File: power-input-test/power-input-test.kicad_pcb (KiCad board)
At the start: 2 copper layers, 19 x 27.3 mm, 15 parts, among them J1 USB_C_Receptacle_USB2.0, J2 Conn_01x06, J3 Conn_01x02, Q1 AO3401A, Q2 AO3402, U1 USBLC6-2SC6, U2 AP2127K-3.3

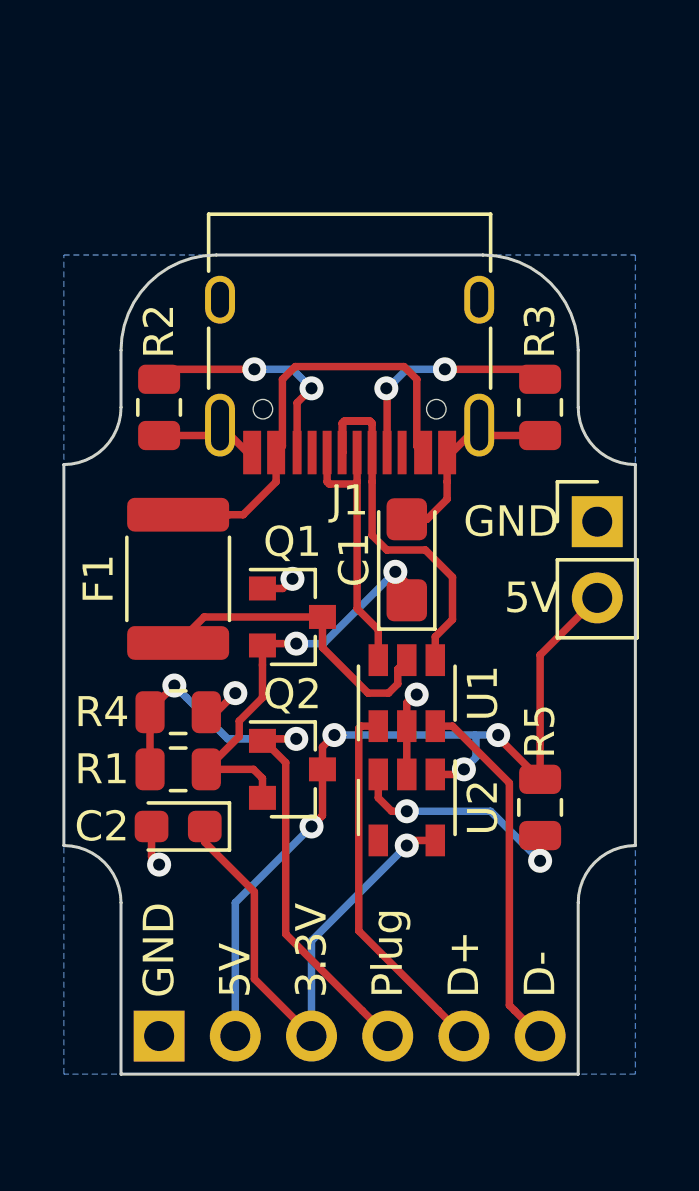
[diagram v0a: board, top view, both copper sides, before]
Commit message: Rev2 power input
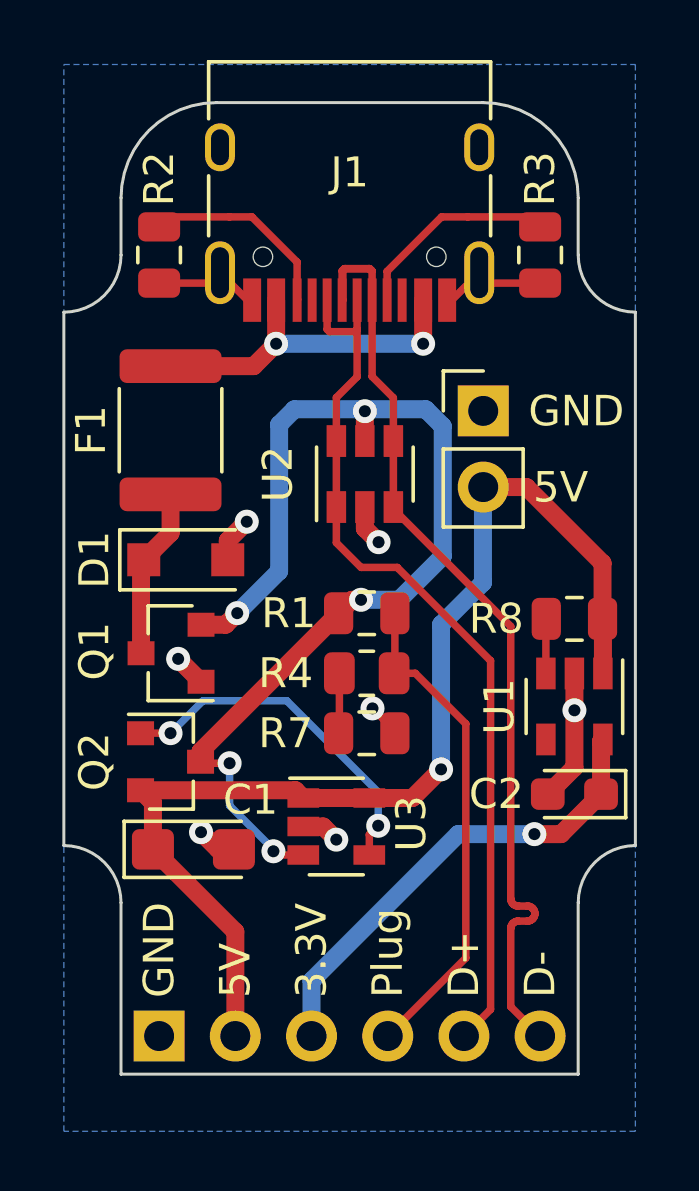
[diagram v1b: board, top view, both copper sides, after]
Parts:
- removed R5: 51k, Resistor_SMD:R_0805_2012Metric
- added D1: SMF5.0CA, Diode_SMD:D_SOD-123F, F.Cu at (94.2, 62.2)
- added R7: 100k, Resistor_SMD:R_0805_2012Metric, F.Cu at (100.3, 68.0)
- added R8: 5.1k, Resistor_SMD:R_0805_2012Metric, F.Cu at (107.2, 64.2)
- added U3: LMV321, Package_TO_SOT_SMD:SOT-23-5, F.Cu at (99.3, 71.1)
- C1: value 100u -> 10u
- Q2: value AO3402 -> AO3401A
- R1: value 51k -> 100k
- U1: value USBLC6-2SC6 -> AP2127K-3.3; footprint Package_TO_SOT_SMD:SOT-23-6 -> Package_TO_SOT_SMD:SOT-23-5
- U2: value AP2127K-3.3 -> AZC199-04S; footprint Package_TO_SOT_SMD:SOT-23-5 -> Package_TO_SOT_SMD:SOT-23-6
- moved C2 13.3 mm to (107.2, 70.0)
- moved C1 12.0 mm to (94.5, 71.9), turned to 0 degrees
- moved U2 11.2 mm to (100.2, 59.4), turned to 90 degrees
- moved R1 8.16 mm to (100.3, 64.0), turned to 0 degrees
- moved R4 6.42 mm to (100.3, 66.0), turned to 180 degrees
- moved U1 5.61 mm to (107.2, 67.1), turned to 270 degrees
- moved J3 5.30 mm to (104.1, 57.3)
- moved J1 5.08 mm to (99.7, 49.5)
- moved R2 5.08 mm to (93.3, 52.1)
- moved R3 5.08 mm to (106.0, 52.1)
- moved F1 4.96 mm to (93.7, 57.9)
- moved Q1 4.22 mm to (93.7, 65.3), turned to 180 degrees
- moved Q2 4.07 mm to (93.7, 69.0)
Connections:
- C1 pad 1: Net-(C1-Pad1) -> +5V
- F1 pad 1: Net-(F1-Pad1) -> Net-(D1-Pad1)
- J1 pad A6: Net-(J1-PadA6) -> D+
- J1 pad A7: Net-(J1-PadA7) -> D-
- J1 pad B6: Net-(J1-PadA6) -> D+
- J1 pad B7: Net-(J1-PadA7) -> D-
- Q1 pad 2: Net-(C1-Pad1) -> Net-(Q1-Pad2)
- Q1 pad 3: Net-(F1-Pad1) -> Net-(D1-Pad1)
- Q2 pad 1: PlugDetect -> Net-(Q2-Pad1)
- Q2 pad 2: Net-(C1-Pad1) -> +5V
- Q2 pad 3: +5V -> Net-(Q1-Pad2)
- R1 pad 1: Net-(C1-Pad1) -> Net-(Q1-Pad2)
- R4 pad 2: GND -> Net-(R4-Pad2)
- U1 pad 1: D+ -> +5V
- U1 pad 3: D- -> Net-(R8-Pad1)
- U1 pad 4: Net-(J1-PadA7) -> (no net)
- U1 pad 5: Net-(F1-Pad1) -> +3V3
- U2 pad 1: +5V -> D+
- U2 pad 3: Net-(R5-Pad1) -> D-
- U2 pad 4: (no net) -> D-
- U2 pad 5: +3V3 -> Net-(Q1-Pad2)
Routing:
- net Net-(Q1-Pad2): track 0.00 -> 36.2 mm, vias 0 -> 5
- net D-: track 12.1 -> 33.1 mm
- net D+: track 12.4 -> 30.1 mm
- net Net-(C1-Pad1): track 14.1 -> 0.00 mm, vias 2 -> 0
- net Net-(J1-PadA7): track 14.0 -> 0.00 mm
- net Net-(Q2-Pad1): track 0.00 -> 11.8 mm, vias 0 -> 2
- net +5V: track 28.1 -> 38.7 mm, vias 4 -> 1
- net Net-(F1-Pad1): track 10.4 -> 0.00 mm
- net Net-(J1-PadA6): track 9.25 -> 0.00 mm
- net Net-(R5-Pad1): track 7.88 -> 0.00 mm, vias 2 -> 0
- net Net-(D1-Pad1): track 0.00 -> 5.70 mm
- net PlugDetect: track 20.7 -> 16.6 mm, vias 2 -> 0
- net Net-(F1-Pad2): track 14.6 -> 11.6 mm, vias 0 -> 2
- net GND: track 17.0 -> 19.3 mm, vias 4 -> 7
- net Net-(R4-Pad2): track 0.00 -> 2.01 mm
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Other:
- board size 19 x 27.3 mm -> 19 x 32.4 mm

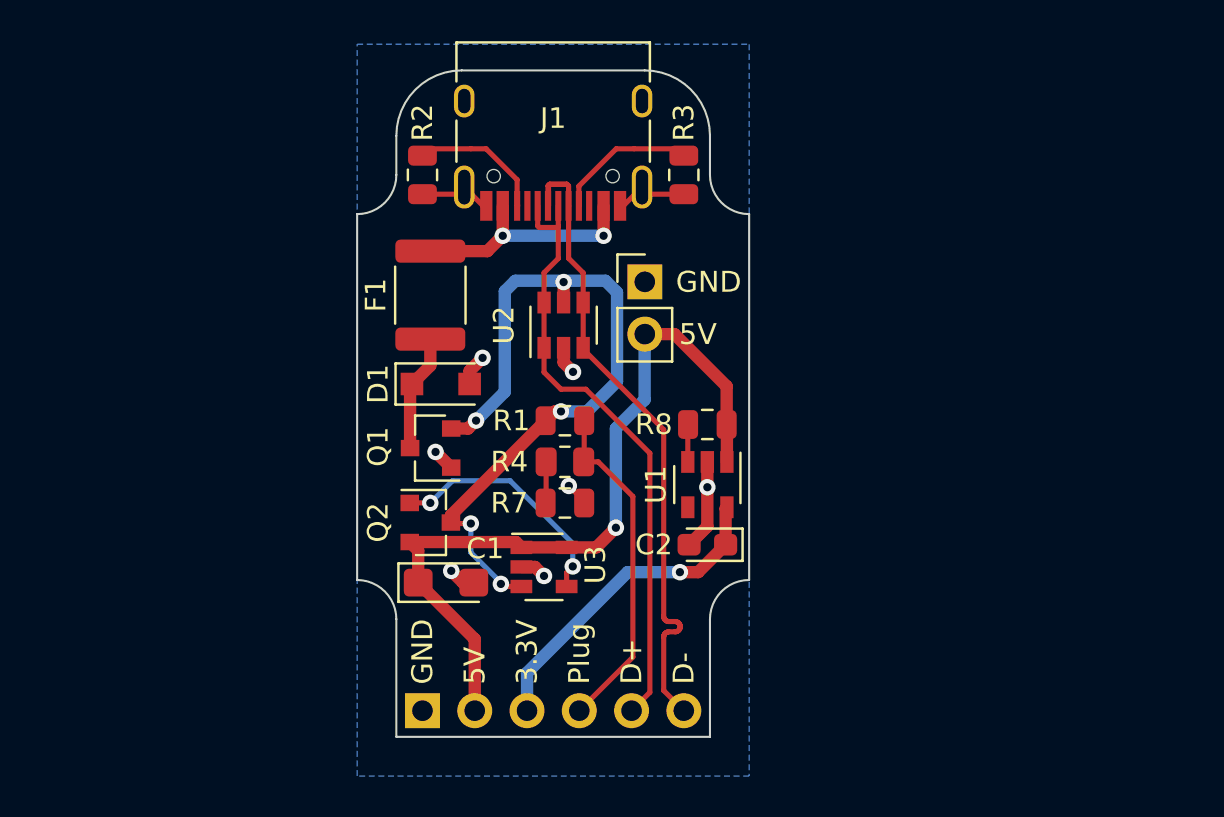
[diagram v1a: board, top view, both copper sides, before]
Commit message: Added defective micromod-reset circuit, untested EVQ circuit.
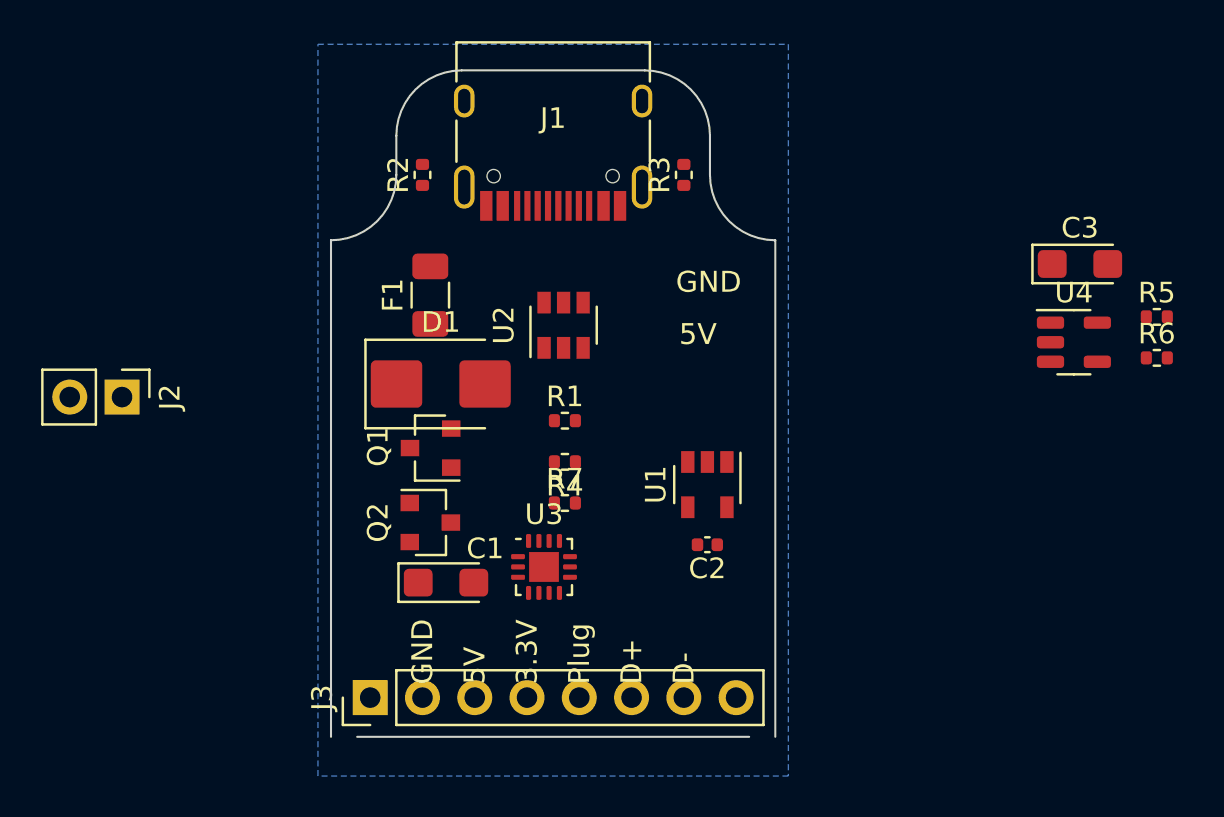
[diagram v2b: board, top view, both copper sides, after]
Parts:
- removed R8: 5.1k, Resistor_SMD:R_0805_2012Metric
- added C3: 10u, Capacitor_Tantalum_SMD:CP_EIA-3216-12_Kemet-S, F.Cu at (125.3, 56.4)
- added R5: 4.7k, Resistor_SMD:R_0402_1005Metric, F.Cu at (129.0, 59.0)
- added R6: 4.7k, Resistor_SMD:R_0402_1005Metric, F.Cu at (129.0, 61.0)
- added U4: AP2127K-3.3, Package_TO_SOT_SMD:SOT-23-5, F.Cu at (125.0, 60.2)
- C2: value 10u -> 100n; footprint Capacitor_Tantalum_SMD:CP_EIA-2012-12_Kemet-R -> Capacitor_SMD:C_0402_1005Metric
- D1: footprint Diode_SMD:D_SOD-123F -> Diode_SMD:D_SMB
- F1: value 3.0A 1812 Polyfuse -> 3.0A Polyfuse; footprint Fuse:Fuse_1812_4532Metric -> Fuse:Fuse_1206_3216Metric
- J2: value Conn_01x06 -> Conn_01x02; footprint Connector_PinHeader_2.54mm:PinHeader_1x06_P2.54mm_Vertical -> Connector_PinHeader_2.54mm:PinHeader_1x02_P2.54mm_Vertical; moved to F.Cu
- J3: value Conn_01x02 -> Conn_01x08; footprint Connector_PinHeader_2.54mm:PinHeader_1x02_P2.54mm_Vertical -> Connector_PinHeader_2.54mm:PinHeader_1x08_P2.54mm_Vertical
- R1: footprint Resistor_SMD:R_0805_2012Metric -> Resistor_SMD:R_0402_1005Metric
- R2, R3: value 5.1k -> 100k; footprint Resistor_SMD:R_0805_2012Metric -> Resistor_SMD:R_0402_1005Metric
- R4, R7: value 100k -> 4.7k; footprint Resistor_SMD:R_0805_2012Metric -> Resistor_SMD:R_0402_1005Metric
- U1: value AP2127K-3.3 -> LMV321
- U3: value LMV321 -> FUSB302BMPX; footprint Package_TO_SOT_SMD:SOT-23-5 -> Package_DFN_QFN:WQFN-14-1EP_2.5x2.5mm_P0.5mm_EP1.45x1.45mm
- moved J3 24.2 mm to (90.8, 77.5), turned to 90 degrees
- moved J2 21.1 mm to (78.7, 62.9)
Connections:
- C2 pad 1: +3V3 -> +3.3V
- J1 pad A5: Net-(J1-PadA5) -> CC1
- J1 pad A8: (no net) -> unconnected-(J1-SBU1-PadA8)
- J1 pad B5: Net-(J1-PadB5) -> CC2
- J1 pad B8: (no net) -> unconnected-(J1-SBU2-PadB8)
- Q1 pad 2: Net-(Q1-Pad2) -> Net-(Q1-S)
- Q2 pad 1: Net-(Q2-Pad1) -> Net-(Q2-G)
- Q2 pad 3: Net-(Q1-Pad2) -> Net-(Q1-S)
- R1 pad 1: Net-(Q1-Pad2) -> Net-(Q1-S)
- R2 pad 1: GND -> PlugDetect
- R2 pad 2: Net-(J1-PadB5) -> Net-(R2-Pad2)
- R3 pad 1: GND -> Net-(R2-Pad2)
- R3 pad 2: Net-(J1-PadA5) -> GND
- R4 pad 1: PlugDetect -> +3.3V
- R4 pad 2: Net-(R4-Pad2) -> SCL
- R7 pad 1: Net-(R4-Pad2) -> Net-(U4-EN)
- R7 pad 2: GND -> +5V
- U1 pad 3: Net-(R8-Pad1) -> Net-(Q1-S)
- U1 pad 4: (no net) -> Net-(Q2-G)
- U1 pad 5: +3V3 -> +5V
- U2 pad 3: D- -> CC2
- U2 pad 5: Net-(Q1-Pad2) -> Net-(Q1-S)
- U2 pad 6: D+ -> CC1
- U3 pad 1: +5V -> CC2
- U3 pad 2: GND -> Net-(Q1-S)
- U3 pad 3: Net-(Q1-Pad2) -> +3.3V
- U3 pad 4: Net-(Q2-Pad1) -> +3.3V
- U3 pad 5: +5V -> Net-(U3-INT_N)
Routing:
- net +5V: track 38.7 -> 0.00 mm, vias 1 -> 0
- net Net-(Q1-Pad2): track 36.2 -> 0.00 mm, vias 5 -> 0
- net D-: track 33.1 -> 0.00 mm
- net D+: track 30.1 -> 0.00 mm
- net GND: track 19.3 -> 0.00 mm, vias 7 -> 0
- net PlugDetect: track 16.6 -> 0.00 mm
- net +3V3: track 15.9 -> 0.00 mm, vias 1 -> 0
- net Net-(Q2-Pad1): track 11.8 -> 0.00 mm, vias 2 -> 0
- net Net-(F1-Pad2): track 11.6 -> 0.00 mm, vias 2 -> 0
- net Net-(J1-PadA5): track 6.95 -> 0.00 mm
- net Net-(J1-PadB5): track 6.66 -> 0.00 mm
- net Net-(D1-A1): track 5.70 -> 0.00 mm
- net Net-(R4-Pad2): track 2.01 -> 0.00 mm
- net Net-(R8-Pad1): track 1.83 -> 0.00 mm
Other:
- board size 19 x 32.4 mm -> 21.6 x 32.4 mm
- net class Default removed
